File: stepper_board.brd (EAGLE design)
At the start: 100 x 80 mm, 60 parts, among them IC1 MCP1703DB, Y1 12 MHz

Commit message: Added ESD Protection and STM documentation
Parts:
- removed R4, R7: 560, rcl:R0805
- removed R5, R6: 22, rcl:R0805
- added D4: ES2D, diode:SMB
- added U$1: DSILC6-4P6, Stepper_Driver:SOT-666
- added U2: MIC2005A-1YM5, Power_Switch:SOT23-5
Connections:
- removed net N$18: R4.2, U1.VBUS1
- removed net N$19: R5.2, U1.D-1
- removed net N$20: R6.2, U1.D+1
- removed net N$21: R7.2, U1.ID1
- net GND: now also U$1.GND, U2.2
- net USB_DM: now also U$1.I/O3, U1.D-1; no longer R5.1
- net USB_DP: now also U$1.I/O2, U1.D+1; no longer R6.1
- net USB_ID: now also U$1.I/O1, U1.ID1; no longer R7.1
- net USB_VBUS: now also D4.A, U$1.VCC, U1.VBUS1, U2.5; no longer R4.1
- net V+: now also D4.C, U2.1
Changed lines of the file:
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@@
 <?xml version="1.0" encoding="utf-8"?>
 <!DOCTYPE eagle SYSTEM "eagle.dtd">
-<eagle version="7.7.0">
+<eagle version="6.6.0">
 <drawing>
 <settings>
@@
 <pass name="Default">
 <param name="RoutingGrid" value="50mil"/>
-<param name="AutoGrid" value="1"/>
-<param name="Efforts" value="0"/>
-<param name="TopRouterVariant" value="1"/>
 <param name="tpViaShape" value="round"/>
-<param name="PrefDir.1" value="a"/>
+<param name="PrefDir.1" value="|"/>
 <param name="PrefDir.2" value="0"/>
 <param name="PrefDir.3" value="0"/>
@@
 <param name="PrefDir.14" value="0"/>
 <param name="PrefDir.15" value="0"/>
-<param name="PrefDir.16" value="a"/>
+<param name="PrefDir.16" value="-"/>
 <param name="cfVia" value="8"/>
 <param name="cfNonPref" value="5"/>
@@
 <element name="R2" library="resistor" package="R0805" value="100" x="59.69" y="15.24"/>
 <element name="R3" library="resistor" package="R0805" value="100" x="81.28" y="15.24"/>
-<element name="R4" library="rcl" package="R0805" value="560" x="80.01" y="35.56"/>
-<element name="R5" library="rcl" package="R0805" value="22" x="80.01" y="41.91"/>
-<element name="R6" library="rcl" package="R0805" value="22" x="80.01" y="48.26"/>
-<element name="R7" library="rcl" package="R0805" value="560" x="80.01" y="54.61"/>
 <element name="R8" library="rcl" package="R0805" value="100k" x="41.91" y="57.15"/>
 <element name="SD1" library="SCHA5B0200_hand" package="SCHA5B0200" value="SCHA5B0200" x="92.71" y="68.58" rot="R90">
@@
 <element name="U1" library="MicroUSB" package="USB-MICRO-SMD" value="" x="91.44" y="46.99" rot="R180"/>
 <element name="Y1" library="abracon" package="3.2X2.5MM" value="12 MHz" x="54.61" y="72.39"/>
+<element name="U$1" library="Stepper_Driver" package="SOT-666" value="DSILC6-4P6" x="-2.54" y="2.54"/>
+<element name="U2" library="Power_Switch" package="SOT23-5" value="MIC2005A-1YM5" x="-1.27" y="-3.81">
+<attribute name="RS" value="727-4731" x="-1.27" y="-3.81" size="1.778" layer="27" display="off"/>
+</element>
+<element name="D4" library="diode" package="SMB" value="ES2D" x="0" y="-11.43"/>
 </elements>
 <signals>
@@
 <contactref element="SD1" pad="VSS"/>
 <contactref element="SD1" pad="CD_SW"/>
-<contactref element="U1" pad="GND1"/>
 <contactref element="C30" pad="2"/>
 <contactref element="R8" pad="1"/>
@@
 <vertex x="99.06" y="78.74"/>
 </polygon>
+<contactref element="U1" pad="GND1"/>
+<contactref element="U$1" pad="GND"/>
+<contactref element="U2" pad="2"/>
 <wire x1="79.16" y1="72.355" x2="90.745" y2="76.03" width="0" layer="19" extent="1-1"/>
 <wire x1="75.88" y1="74.93" x2="79.16" y2="72.355" width="0" layer="19" extent="1-1"/>
@@
 <wire x1="82.23" y1="10.16" x2="78.31" y2="19.285" width="0" layer="19" extent="1-1"/>
 <wire x1="82.55" y1="2.54" x2="82.23" y2="10.16" width="0" layer="19" extent="1-1"/>
-<wire x1="60.64" y1="10.16" x2="60.96" y2="2.54" width="0" layer="19" extent="1-1"/>
-<wire x1="41.59" y1="10.16" x2="41.91" y2="2.54" width="0" layer="19" extent="1-1"/>
-<wire x1="11.11" y1="12.7" x2="11.43" y2="2.54" width="0" layer="19" extent="1-1"/>
-<wire x1="6.21" y1="21.59" x2="11.11" y2="12.7" width="0" layer="19" extent="1-1"/>
 <wire x1="44.13" y1="29.21" x2="52.91" y2="21.885" width="0" layer="19" extent="1-1"/>
 <wire x1="37.78" y1="29.21" x2="44.13" y2="29.21" width="0" layer="19" extent="1-1"/>
@@
 <wire x1="27.51" y1="21.885" x2="30.48" y2="22.86" width="0" layer="19" extent="1-1"/>
 <wire x1="27.51" y1="19.285" x2="27.51" y2="21.885" width="0" layer="19" extent="1-1"/>
+<wire x1="60.64" y1="10.16" x2="52.91" y2="19.285" width="0" layer="19" extent="1-1"/>
+<wire x1="60.96" y1="2.54" x2="60.64" y2="10.16" width="0" layer="19" extent="1-1"/>
+<wire x1="41.59" y1="10.16" x2="52.91" y2="19.285" width="0" layer="19" extent="1-1"/>
+<wire x1="41.91" y1="2.54" x2="41.59" y2="10.16" width="0" layer="19" extent="1-1"/>
 <wire x1="88.74" y1="48.29" x2="79.16" y2="62.605" width="0" layer="19" extent="1-1"/>
+<wire x1="11.11" y1="12.7" x2="27.51" y2="19.285" width="0" layer="19" extent="1-1"/>
+<wire x1="6.21" y1="21.59" x2="11.11" y2="12.7" width="0" layer="19" extent="1-1"/>
+<wire x1="11.43" y1="2.54" x2="11.11" y2="12.7" width="0" layer="19" extent="1-1"/>
+<wire x1="13.97" y1="2.54" x2="11.43" y2="2.54" width="0" layer="19" extent="1-1"/>
+<wire x1="-1.27" y1="-5.1101" x2="11.43" y2="2.54" width="0" layer="19" extent="1-1"/>
+<wire x1="-3.66" y1="2.56" x2="-1.27" y2="-5.1101" width="0" layer="19" extent="1-1"/>
 </signal>
 <signal name="1_OUT1A">
@@
 <contactref element="IC1" pad="1"/>
 <contactref element="C16" pad="1"/>
+<contactref element="D4" pad="C"/>
+<contactref element="U2" pad="1"/>
 <wire x1="16.83" y1="54.61" x2="21.8186" y2="57.8612" width="0" layer="19" extent="1-1"/>
+<wire x1="-2.22" y1="-5.1101" x2="16.83" y2="54.61" width="0" layer="19" extent="1-1"/>
+<wire x1="-2.2" y1="-11.43" x2="-2.22" y2="-5.1101" width="0" layer="19" extent="1-1"/>
 </signal>
 <signal name="SD_D1">
@@
 <signal name="USB_DP">
 <contactref element="STM32F411RE" pad="45"/>
-<contactref element="R6" pad="1"/>
-<wire x1="55.59" y1="55.21" x2="79.06" y2="48.26" width="0" layer="19" extent="1-1"/>
+<contactref element="U1" pad="D+1"/>
+<contactref element="U$1" pad="I/O2"/>
+<wire x1="55.59" y1="55.21" x2="88.74" y2="46.99" width="0" layer="19" extent="1-1"/>
+<wire x1="-3.66" y1="2.06" x2="55.59" y2="55.21" width="0" layer="19" extent="1-1"/>
 </signal>
 <signal name="USB_DM">
 <contactref element="STM32F411RE" pad="44"/>
-<contactref element="R5" pad="1"/>
-<wire x1="55.09" y1="55.21" x2="79.06" y2="41.91" width="0" layer="19" extent="1-1"/>
+<contactref element="U1" pad="D-1"/>
+<contactref element="U$1" pad="I/O3"/>
+<wire x1="55.09" y1="55.21" x2="88.74" y2="46.34" width="0" layer="19" extent="1-1"/>
+<wire x1="-1.42" y1="2.06" x2="55.09" y2="55.21" width="0" layer="19" extent="1-1"/>
 </signal>
 <signal name="USB_ID">
 <contactref element="STM32F411RE" pad="43"/>
-<contactref element="R7" pad="1"/>
-<wire x1="54.59" y1="55.21" x2="79.06" y2="54.61" width="0" layer="19" extent="1-1"/>
+<contactref element="U1" pad="ID1"/>
+<contactref element="U$1" pad="I/O1"/>
+<wire x1="54.59" y1="55.21" x2="88.74" y2="47.64" width="0" layer="19" extent="1-1"/>
+<wire x1="-3.66" y1="3.06" x2="54.59" y2="55.21" width="0" layer="19" extent="1-1"/>
 </signal>
 <signal name="USB_VBUS">
 <contactref element="STM32F411RE" pad="42"/>
-<contactref element="R4" pad="1"/>
-<wire x1="54.09" y1="55.21" x2="79.06" y2="35.56" width="0" layer="19" extent="1-1"/>
-</signal>
-<signal name="N$18">
-<contactref element="R4" pad="2"/>
 <contactref element="U1" pad="VBUS1"/>
-<wire x1="80.96" y1="35.56" x2="88.74" y2="45.69" width="0" layer="19" extent="1-1"/>
-</signal>
-<signal name="N$19">
-<contactref element="R5" pad="2"/>
-<contactref element="U1" pad="D-1"/>
-<wire x1="80.96" y1="41.91" x2="88.74" y2="46.34" width="0" layer="19" extent="1-1"/>
-</signal>
-<signal name="N$20">
-<contactref element="R6" pad="2"/>
-<contactref element="U1" pad="D+1"/>
-<wire x1="80.96" y1="48.26" x2="88.74" y2="46.99" width="0" layer="19" extent="1-1"/>
-</signal>
-<signal name="N$21">
-<contactref element="R7" pad="2"/>
-<contactref element="U1" pad="ID1"/>
-<wire x1="88.74" y1="47.64" x2="80.96" y2="54.61" width="0" layer="19" extent="1-1"/>
+<contactref element="U$1" pad="VCC"/>
+<contactref element="U2" pad="5"/>
+<contactref element="D4" pad="A"/>
+<wire x1="54.09" y1="55.21" x2="88.74" y2="45.69" width="0" layer="19" extent="1-1"/>
+<wire x1="-1.42" y1="2.56" x2="54.09" y2="55.21" width="0" layer="19" extent="1-1"/>
+<wire x1="-2.22" y1="-2.5099" x2="-1.42" y2="2.56" width="0" layer="19" extent="1-1"/>
+<wire x1="2.2" y1="-11.43" x2="-2.22" y2="-2.5099" width="0" layer="19" extent="1-1"/>
 </signal>
 <signal name="N$22">

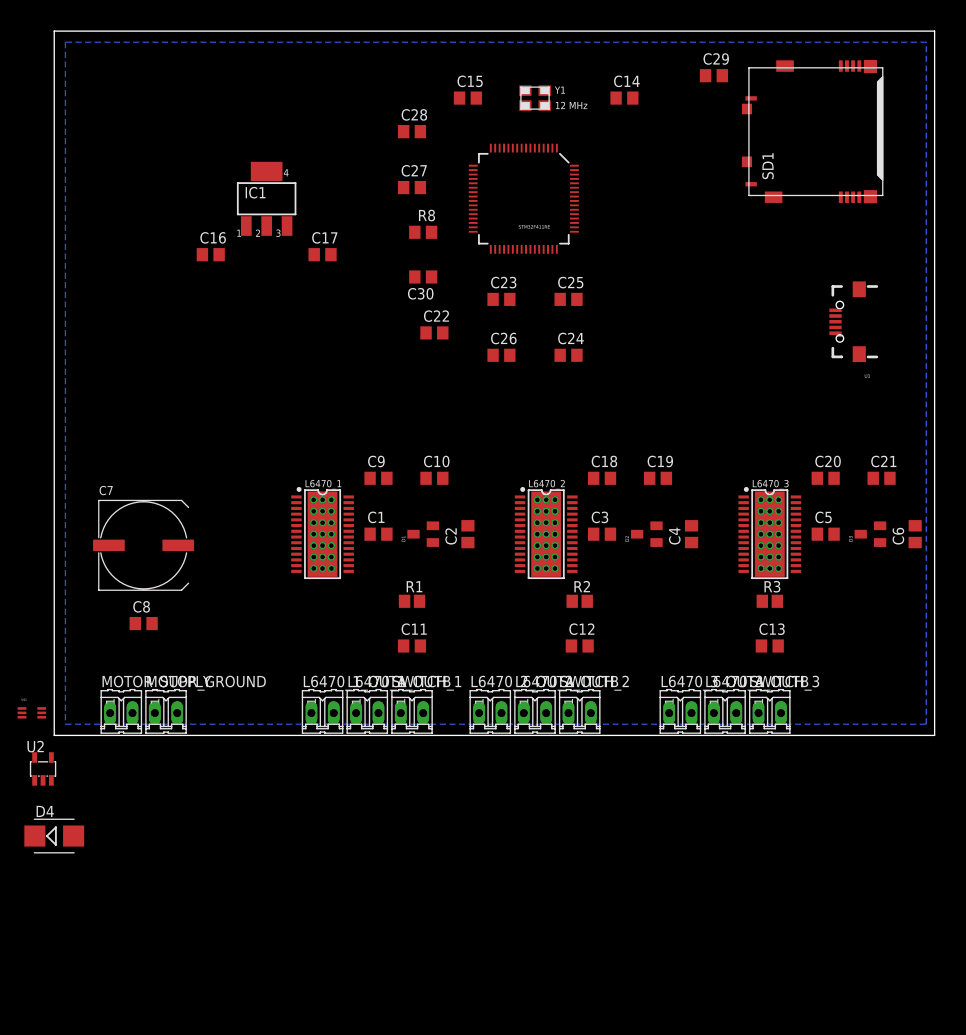
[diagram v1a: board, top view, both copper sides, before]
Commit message: Tried to start unraveling the rats' nest.
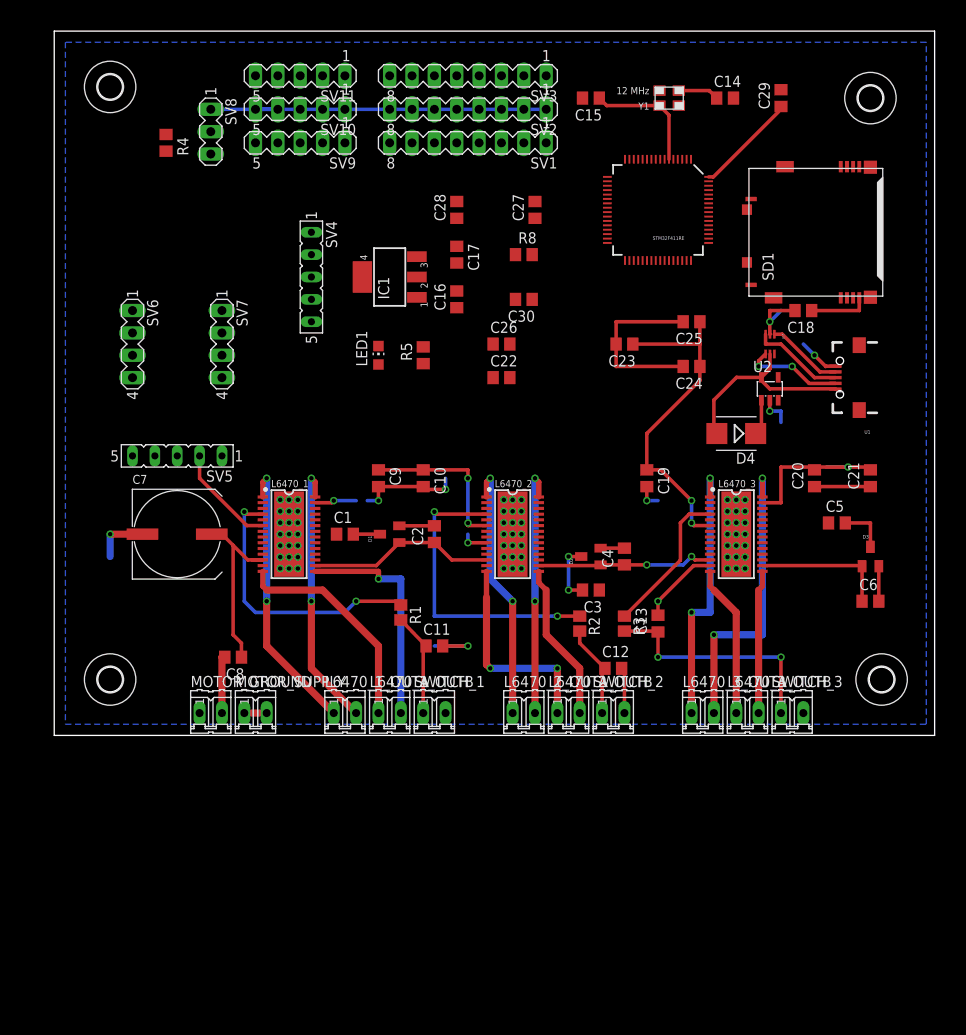
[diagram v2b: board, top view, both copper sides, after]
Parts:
- added LED1: (no value), led:CHIP-LED0805
- added R4: 100k, rcl:R0805
- added R5: 560, rcl:R0805
- added SV1, SV2, SV3: (no value), con-lstb:MA08-1
- added SV10, SV11, SV9: (no value), con-lstb:MA05-1
- added SV4, SV5: (no value), con-lsta:FE05-1
- added SV6, SV7: (no value), con-lstb:MA04-1
- added SV8: (no value), con-lstb:MA03-1
- added U$2, U$3, U$4, U$5: (no value), holes:2,8
- moved U$1 93.7 mm to (81.3, 44.5), turned to 270 degrees
- moved U2 93.2 mm to (81.3, 39.4)
- moved D4 90.0 mm to (77.5, 34.3), turned to 180 degrees
- moved C18 29.8 mm to (85.1, 48.3), turned to 180 degrees
- moved C16 28.4 mm to (45.7, 49.5), turned to 90 degrees
- moved R3 16.7 mm to (64.8, 12.7), turned to 270 degrees
- moved IC1 16.6 mm to (38.1, 52.1), turned to 90 degrees
- moved STM32F411RE 15.3 mm to (68.6, 59.7)
- moved C17 15.2 mm to (45.7, 54.6), turned to 270 degrees
- moved MOTOR_SUPPLY 15.2 mm to (22.9, 2.54)
- moved Y1 15.2 mm to (69.8, 72.4), turned to 180 degrees
- moved C23 14.9 mm to (64.8, 44.5), turned to 180 degrees
- moved C25 14.2 mm to (72.4, 47.0), turned to 180 degrees
- moved C27 14.2 mm to (54.6, 59.7), turned to 90 degrees
- moved C24 14.0 mm to (72.4, 41.9), turned to 180 degrees
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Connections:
- new net ADC0: SV1.1
- new net ADC1: STM32F411RE.15, SV1.2
- new net ADC1_14: STM32F411RE.24
- new net ADC1_15: STM32F411RE.25
- new net ADC2: STM32F411RE.16, SV1.3
- new net ADC3: STM32F411RE.17, SV1.4
- new net ADC4: STM32F411RE.20, SV1.5
- new net ADC5: STM32F411RE.21, SV1.6
- new net ADC6: SV1.7
- new net ADC7: STM32F411RE.23, SV1.8
- new net BUSY1: L6470_1.22, STM32F411RE.34
- new net BUSY2: L6470_2.22, STM32F411RE.36
- new net BUSY3: L6470_3.22, STM32F411RE.38
- new net FLAG1: L6470_1.24, STM32F411RE.33
- new net FLAG2: L6470_2.24, STM32F411RE.35
- new net FLAG3: L6470_3.24, STM32F411RE.37
- new net GPIO0: SV9.1
- new net GPIO1: STM32F411RE.27, SV9.2
- new net GPIO2: STM32F411RE.49, SV9.3
- new net GPIO3: STM32F411RE.50, SV9.4
- new net GPIO4: STM32F411RE.41, SV9.5
- new net I2C1_SCL: STM32F411RE.61, SV6.4
- new net I2C1_SDA: STM32F411RE.62, SV6.3
- new net JSSW: STM32F411RE.46, SV4.5
- new net JSX: STM32F411RE.8, SV4.3
- new net JSY: STM32F411RE.9, SV4.4
- new net N$18: STM32F411RE.60, SV8.2
- new net N$19: R4.2, SV8.3
- new net N$20: LED1.A, R5.1
- new net OSC32_IN: STM32F411RE.3, SV5.4
- new net OSC32_OUT: STM32F411RE.4, SV5.5
- new net OSCIN1: L6470_1.7
- new net OSCIN2: L6470_2.7
- new net OSCOUT1: L6470_1.8
- new net OSCOUT2: L6470_2.8
- new net OSCOUT3: L6470_3.8
- new net RESET: L6470_2.3, L6470_3.3, STM32F411RE.7
- new net RTC: STM32F411RE.2, SV5.3
- new net SPI2_MOSI: STM32F411RE.11
- new net SPI2_SCK: STM32F411RE.29
- new net STCK1: L6470_1.25
- new net STCK2: L6470_2.25
- new net STCK3: L6470_3.25
- new net USART1_RX: STM32F411RE.59, SV7.3
- new net USART1_TX: STM32F411RE.58, SV7.4
- net +3V3: now also R5.2, SV10.1, SV10.2, SV10.3, SV10.4, SV10.5, SV2.1, SV2.2, SV2.3, SV2.4, SV2.5, SV2.6, SV2.7, SV2.8, SV4.2, SV5.2, SV6.2, SV7.2, SV8.1
- net GND: now also LED1.C, R4.1, SV11.1, SV11.2, SV11.3, SV11.4, SV11.5, SV3.1, SV3.2, SV3.3, SV3.4, SV3.5, SV3.6, SV3.7, SV3.8, SV4.1, SV5.1, SV6.1, SV7.1
- net SPI1_MISO: now also STM32F411RE.56; no longer STM32F411RE.22
- net SPI1_MOSI: now also STM32F411RE.57; no longer STM32F411RE.23
- net SPI1_SCK: now also STM32F411RE.55; no longer STM32F411RE.21
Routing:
- net +3V3: track 0.00 -> 133.7 mm, vias 0 -> 4
- net GND: track 0.00 -> 112.1 mm, vias 0 -> 12
- net VCC: track 0.00 -> 80.0 mm, vias 0 -> 2
- net N$12: track 0.00 -> 34.4 mm, vias 0 -> 2
- net 3_OUT2A: track 0.00 -> 34.3 mm, vias 0 -> 2
- net 1_OUT1A: track 0.00 -> 32.1 mm, vias 0 -> 2
- net N$7: track 0.00 -> 31.6 mm, vias 0 -> 2
- net 1_OUT2A: track 0.00 -> 31.1 mm, vias 0 -> 2
- net 3_OUT1A: track 0.00 -> 30.9 mm, vias 0 -> 2
- net 2_OUT1A: track 0.00 -> 30.0 mm, vias 0 -> 2
- net 2_OUT2A: track 0.00 -> 29.0 mm, vias 0 -> 2
- net N$15: track 0.00 -> 27.1 mm, vias 0 -> 2
- net 1_OUT2B: track 0.00 -> 25.8 mm, vias 0 -> 1
- net 1_OUT1B: track 0.00 -> 25.3 mm
- net 2_OUT1B: track 0.00 -> 23.9 mm, vias 0 -> 2
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
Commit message: More wiring in progress
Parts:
- moved C23 9.69 mm to (59.7, 36.2)
- moved C25 9.69 mm to (67.3, 38.7)
- moved C24 9.69 mm to (67.3, 33.7)
- moved C3 8.35 mm to (62.2, 24.8), turned to 0 degrees
- moved U$1 6.87 mm to (75.6, 40.6), turned to 0 degrees
- moved U2 5.39 mm to (85.1, 35.6)
- moved D2 4.62 mm to (65.4, 21.6), turned to 0 degrees
- moved C28 3.70 mm to (48.9, 57.8)
- moved C4 3.24 mm to (65.4, 17.1), turned to 0 degrees
- moved C27 3.18 mm to (52.1, 57.8)
- moved D4 3.17 mm to (74.9, 32.4)
- moved C17 2.01 mm to (47.6, 54.0), turned to 180 degrees
- moved C13 1.91 mm to (70.5, 12.7)
- moved C18 1.91 mm to (87.0, 48.3)
- moved C19 1.91 mm to (65.4, 29.2)
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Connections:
- net 3_OUT1A: now also L6470_3_OUTA.2; no longer L6470_3_OUTA.1
- net 3_OUT2A: now also L6470_3_OUTA.1; no longer L6470_3_OUTA.2
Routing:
- net +3V3: track 133.7 -> 260.3 mm, vias 4 -> 5
- net GND: track 112.1 -> 236.7 mm, vias 12 -> 10
- net JSSW: track 0.00 -> 57.2 mm, vias 0 -> 1
- net SPI1_MISO: track 0.00 -> 53.3 mm, vias 0 -> 2
- net SPI1_SCK: track 0.00 -> 50.7 mm, vias 0 -> 2
- net RESET: track 0.00 -> 42.2 mm, vias 0 -> 2
- net SPI1_MOSI: track 0.00 -> 39.0 mm, vias 0 -> 2
- net N$8: track 0.00 -> 38.3 mm, vias 0 -> 2
- net SD_D0: track 0.00 -> 36.1 mm, vias 0 -> 2
- net BUSY3: track 0.00 -> 35.9 mm
- net FLAG3: track 0.00 -> 35.2 mm
- net VCC: track 80.0 -> 113.9 mm, vias 2 -> 5
- net SD_D1: track 0.00 -> 32.7 mm, vias 0 -> 2
- net USB_VBUS: track 22.6 -> 55.1 mm
- net 1_OUT1A: track 32.1 -> 0.00 mm, vias 2 -> 0
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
